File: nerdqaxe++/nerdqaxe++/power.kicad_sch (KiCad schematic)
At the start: 73 parts, among them J3 Conn_01x01, J4 Conn_01x01, U2 TPSM82901SISR, U3 TPS53647, U36 MCP1824T-1202E, U7 MCP1824T-0802E

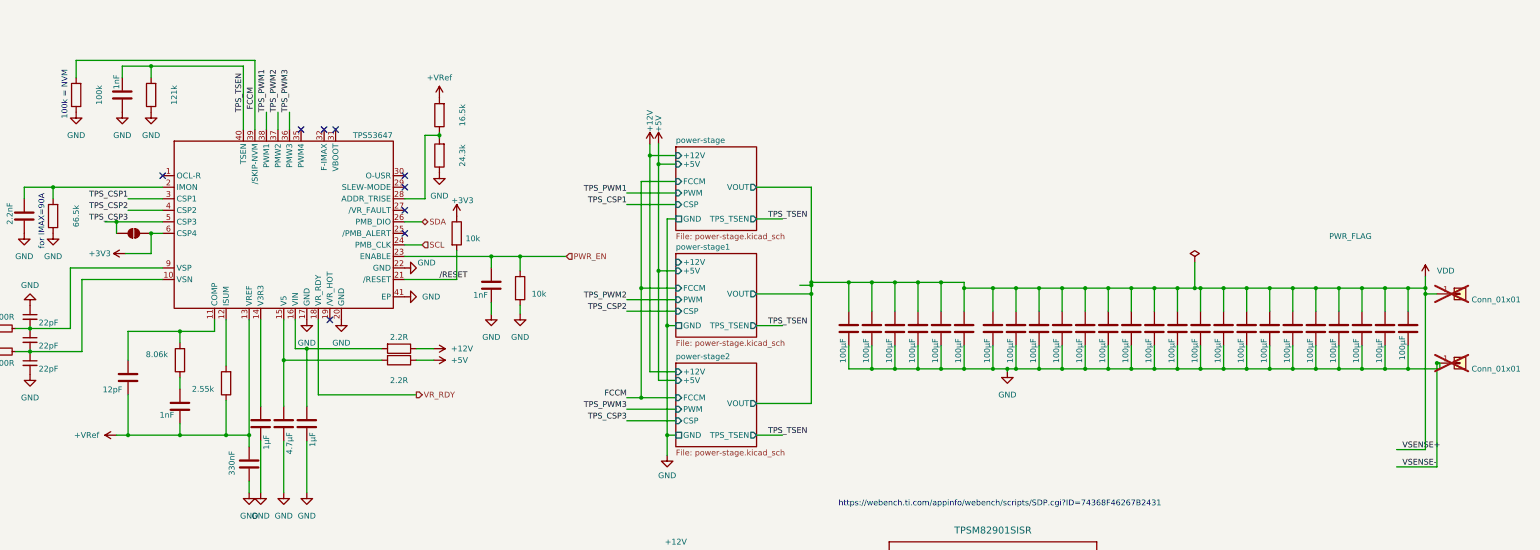
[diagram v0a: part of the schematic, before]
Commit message: Edit on rev 6.1PM
- Moved XT30 connector to the back of the board
- Edited VDD polygon
- Fixed various via placements
- Fixed various tracing
- Updated BM1370 footprint and solder paste stencil
- Updated CSD95472Q5MC footprint and solder paste stencil
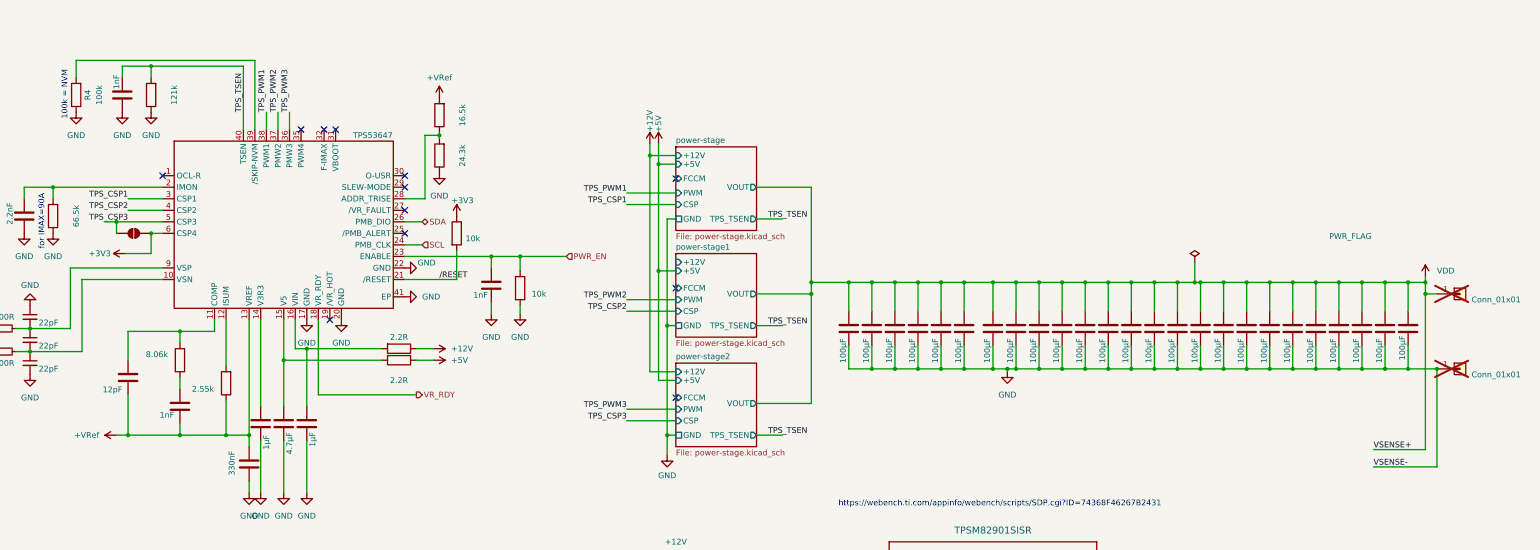
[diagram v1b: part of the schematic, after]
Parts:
- U2: LCSC (none) -> C6290581; PARTNO (none) -> TPSM82901SISR
- U36, U7: Manufacturer  (none) -> Microchip Technology
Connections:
- net FCCM: no longer names the net of R4.2, U3.39 (/SKIP-NVM)
- no-connect marks 12 -> 15
